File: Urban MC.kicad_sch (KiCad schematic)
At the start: 48 parts, among them J1 Conn_01x02, J2 Screw_Terminal_01x02, J3 Conn_01x02, J4 Conn_01x03, J5 Conn_01x02, J6 Screw_Terminal_01x03, SW1 SW_Push, U1 IRS2186, U1 MCP4725xxx-xCH, U2 IRS2186, U2 MCP2515-xSO, U3 IRS2186, U3 TJA1050, U4 IRF150P220XKMA1, U5 IRF150P220XKMA1, U6 IRF150P220XKMA1, U7 IRF150P220XKMA1, U8 IRF150P220XKMA1, U9 IRF150P220XKMA1

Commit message: added custom footprints
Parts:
- removed J6: Screw_Terminal_01x03, symbol Connector:Screw_Terminal_01x03
- added J10, J6, J7, J8, J9: Screw_Terminal_01x01, urban_mc_custom_footprints:WP-SHFU_7461100, symbol Connector:Screw_Terminal_01x01
- D1, D2: footprint (none) -> Diode_THT:D_DO-41_SOD81_P10.16mm_Horizontal
- HallConnectors1: renamed from J4; footprint (none) -> urban_mc_custom_footprints:CON_436500300_MOL
- HallPowerInput1: renamed from J5; footprint (none) -> urban_mc_custom_footprints:CON_436500200_MOL
- J1, J2, J3: footprint (none) -> urban_mc_custom_footprints:CON_436500200_MOL
- U10: footprint urban_mc_custom_footprints:CONV_LCW78_12-0.5 -> urban_mc_custom_footprints:CONV_LCW78_12-1.0
- U4, U5, U6, U7, U8, U9: footprint PG-TO247-3-901_INF -> urban_mc_custom_footprints:PG-TO247-3-901_INF
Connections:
- net +48V: now also J9.1 (Pin_1)
- net GND: now also J10.1 (Pin_1)
- net at R6.2, U6.3 (SOURCE), U7.2 (DRAIN): now also J7.1 (Pin_1)
- net at R7.2, U8.3 (SOURCE), U9.2 (DRAIN): now also J8.1 (Pin_1)
- net at R5.2, U4.3 (SOURCE), U5.2 (DRAIN): now also J6.1 (Pin_1)

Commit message: updated schematic
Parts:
- removed D2: D, Diode_THT:D_DO-41_SOD81_P10.16mm_Horizontal, symbol Device:D
- removed J7, J8: Screw_Terminal_01x01, urban_mc_custom_footprints:WP-SHFU_7461100, symbol Connector:Screw_Terminal_01x01
- removed U2: IRS2186, Package_SO:SOIC-8_3.9x4.9mm_P1.27mm, symbol Driver_FET:IRS2186
- added J4, J5: Screw_Terminal_01x01, urban_mc_custom_footprints:WP-SHFU_7461100, symbol Connector:Screw_Terminal_01x01
- added U14, U15, U16, U17, U18, U19, U2, U20, U21, U22, U24, U25, U26, U27, U28, U29, U30, U31: IQE022N06LM5CGSCATMA1, urban_mc_custom_footprints:IFX-PG-WHTFN-9-1-V, symbol IRF150P220:IRF150P220XKMA1
- added U23: IRS2186, Package_SO:SOIC-8_3.9x4.9mm_P1.27mm, symbol Driver_FET:IRS2186
- C11: value 1u -> 10u; footprint Capacitor_SMD:C_2220_5750Metric -> Capacitor_SMD:C_0805_2012Metric
- C8: value 10u -> 1u; footprint Capacitor_SMD:C_0805_2012Metric -> Capacitor_SMD:C_2220_5750Metric
- R3, R8: value 11Ω -> 2.4Ω; footprint Resistor_SMD:R_0402_1005Metric -> Resistor_SMD:R_0603_1608Metric
- R5, R6: value 2.4Ω -> 11Ω; footprint Resistor_SMD:R_0603_1608Metric -> Resistor_SMD:R_0402_1005Metric
- U1: value MCP4725xxx-xCH -> MCP4725
- U4, U5, U6, U7, U8, U9: value IRF150P220XKMA1 -> IQE022N06LM5CGSCATMA1; footprint urban_mc_custom_footprints:PG-TO247-3-901_INF -> urban_mc_custom_footprints:IFX-PG-WHTFN-9-1-V
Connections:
- net +12V: now also C1.2, U23.5 (VCC); no longer C8.2
- net +48V: now also U5.2 (DRAIN), U14.2 (DRAIN), U15.2 (DRAIN), U16.2 (DRAIN), U2.2 (DRAIN), U24.2 (DRAIN), U25.2 (DRAIN), U26.2 (DRAIN), U27.2 (DRAIN); no longer C11.1, C12.1, C13.1
- net GND: now also C1.1, C8.2, U17.3 (SOURCE), U18.3 (SOURCE), U19.3 (SOURCE), U20.3 (SOURCE), U21.3 (SOURCE), U22.3 (SOURCE), U23.3 (COM), U28.3 (SOURCE), U29.3 (SOURCE), U30.3 (SOURCE), U31.3 (SOURCE); no longer C11.2, C8.1, U5.3 (SOURCE)
- net at U1.8 (VB): now also C2.2; no longer C1.2
- net at R8.2: now also C12.1, J4.1 (Pin_1), U24.3 (SOURCE), U25.3 (SOURCE), U26.3 (SOURCE), U27.3 (SOURCE), U28.2 (DRAIN), U29.2 (DRAIN), U30.2 (DRAIN), U31.2 (DRAIN); no longer U6.1 (GATE)
- net at U6.3 (SOURCE), U7.2 (DRAIN): now also C8.1, R3.2, U4.3 (SOURCE), U5.3 (SOURCE), J5.1 (Pin_1), U2.3 (SOURCE), U20.2 (DRAIN), U21.2 (DRAIN), U22.2 (DRAIN); no longer R6.2
- net at A1.6 (D3): now also U1.1 (HIN)
- net at A1.8 (D5): now also U1.2 (LIN)
- net at R3.1: now also C2.1, U1.6 (VS)
- net at R6.1: now also U23.7 (HO); no longer C2.1
- net at R8.1: now also C11.1, U23.6 (VS)
- net at R4.2, U9.1 (GATE): now also U17.1 (GATE), U18.1 (GATE), U19.1 (GATE)
- net at R7.2, U8.3 (SOURCE), U9.2 (DRAIN): now also C13.1, J6.1 (Pin_1), U14.3 (SOURCE), U15.3 (SOURCE), U16.3 (SOURCE), U17.2 (DRAIN), U18.2 (DRAIN), U19.2 (DRAIN)
- net at R2.2, U5.1 (GATE): now also U4.1 (GATE), U6.1 (GATE), U2.1 (GATE)
- net at R9.1: now also U23.4 (LO); no longer U1.7 (HO)
- net at R9.2: now also U28.1 (GATE), U29.1 (GATE), U30.1 (GATE), U31.1 (GATE); no longer U4.1 (GATE)
- net at U7.1 (GATE): now also R5.2, U20.1 (GATE), U21.1 (GATE), U22.1 (GATE); no longer R3.2
- net at A1.12 (D9): now also U23.2 (LIN); no longer U1.2 (LIN)
- net at A1.9 (D6): now also U23.1 (HIN); no longer U1.1 (HIN)
- net at R10.2, U8.1 (GATE): now also U14.1 (GATE), U15.1 (GATE), U16.1 (GATE)
- net at U1.4 (LO): now also R5.1; no longer R2.1
- new net: R6.2, U24.1 (GATE), U25.1 (GATE), U26.1 (GATE), U27.1 (GATE)
- new net: C11.2, U23.8 (VB)
- new net: R2.1, U1.7 (HO)
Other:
- moved on the sheet: A1, C10, C13, C3, C4, C5, C6, C7, D1, HallConnectors1, HallPowerInput1, J1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

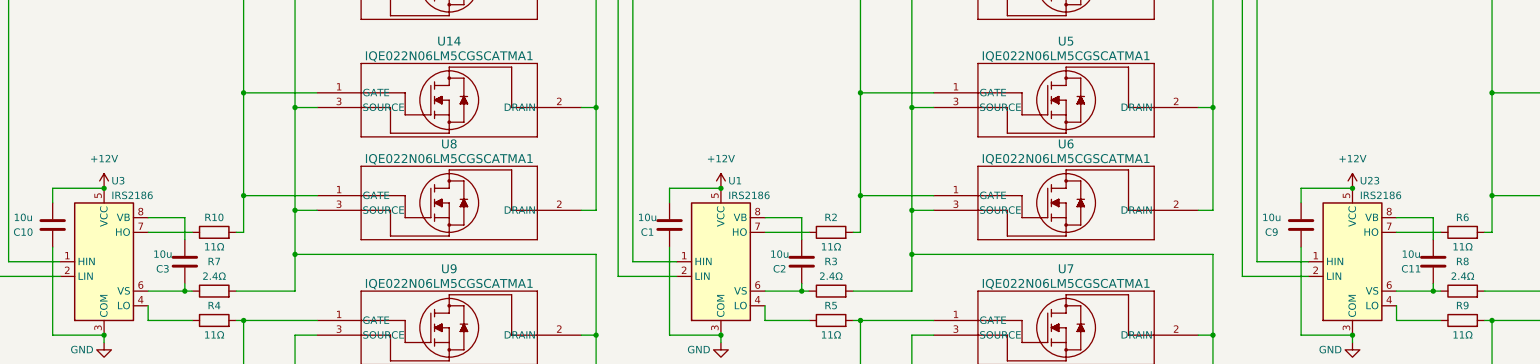
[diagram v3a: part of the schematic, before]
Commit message: Added diodes
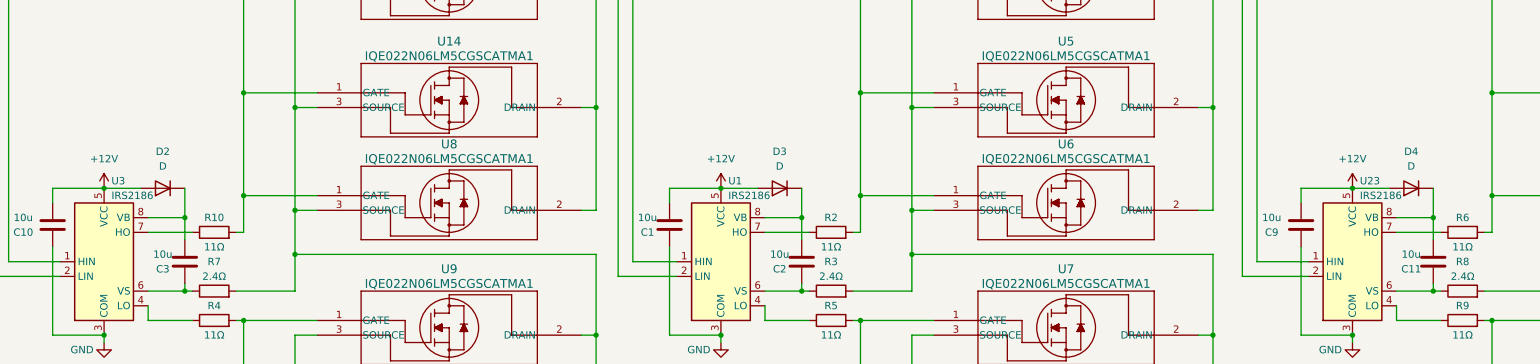
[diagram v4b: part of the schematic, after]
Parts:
- added D2, D3, D4: D, Diode_THT:D_DO-41_SOD81_P10.16mm_Horizontal, symbol Device:D
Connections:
- net +12V: now also D2.2 (A), D3.2 (A), D4.2 (A)
- net at C3.2, U3.8 (VB): now also D2.1 (K)
- net at C11.2, U23.8 (VB): now also D4.1 (K)
- net at C2.2, U1.8 (VB): now also D3.1 (K)

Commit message: Updated mosfet symbol
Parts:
- removed C1, C2: 10u, Capacitor_SMD:C_0805_2012Metric, symbol Device:C
- removed C13: 1u, Capacitor_SMD:C_2220_5750Metric, symbol Device:C
- removed R2: 11Ω, Resistor_SMD:R_0402_1005Metric, symbol Device:R
- removed R3: 2.4Ω, Resistor_SMD:R_0603_1608Metric, symbol Device:R
- removed U1, U23: IRS2186, Package_SO:SOIC-8_3.9x4.9mm_P1.27mm, symbol Driver_FET:IRS2186
- removed U14, U15, U17, U18, U19, U2, U20, U21, U22, U24, U25, U26, U27, U28, U29, U30, U31, U4, U5, U6, U7, U8, U9: IQE022N06LM5CGSCATMA1, urban_mc_custom_footprints:IFX-PG-WHTFN-9-1-V, symbol IRF150P220:IRF150P220XKMA1
- added C10, C7: 10u, Capacitor_SMD:C_0805_2012Metric, symbol Device:C
- added C6: 1u, Capacitor_SMD:C_2220_5750Metric, symbol Device:C
- added Q10, Q11, Q12, Q13, Q14, Q15, Q16, Q17, Q18, Q19, Q2, Q20, Q21, Q22, Q23, Q24, Q3, Q4, Q5, Q6, Q7, Q8, Q9: IQE022N06LM5CGSCATMA1, urban_mc_custom_footprints:IFX-PG-WHTFN-9-1-V, symbol Supermileage Symbols:root_0_IQE022N06LM5CGSC
- added R10, R7: 2.4Ω, Resistor_SMD:R_0603_1608Metric, symbol Device:R
- added U2, U3: IRS2186, Package_SO:SOIC-8_3.9x4.9mm_P1.27mm, symbol Driver_FET:IRS2186
- C8: value 1u -> 10u; footprint Capacitor_SMD:C_2220_5750Metric -> Capacitor_SMD:C_0805_2012Metric
- C9: value 10u -> 1u; footprint Capacitor_SMD:C_0805_2012Metric -> Capacitor_SMD:C_2220_5750Metric
- Q1: renamed from U16; symbol IRF150P220:IRF150P220XKMA1 -> Supermileage Symbols:root_0_IQE022N06LM5CGSC
- R8: value 2.4Ω -> 11Ω; footprint Resistor_SMD:R_0603_1608Metric -> Resistor_SMD:R_0402_1005Metric
- renumbered C4 to C1, C7 to C13, C5 to C2, C6 to C3, C10 to C4, C3 to C5, J9 to J4, J10 to J5, J4 to J6, J5 to J7, J6 to J8, R10 to R2, R7 to R3, U3 to U1
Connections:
- net +12V: now also C10.2, C7.2, U2.5 (VCC), U3.5 (VCC); no longer C9.2
- net +48V: now also Q1.5 (DRAIN1), Q1.6 (DRAIN2), Q1.7 (DRAIN3), Q1.8 (DRAIN4), Q11.5 (DRAIN1), Q11.6 (DRAIN2), Q11.7 (DRAIN3), Q11.8 (DRAIN4), Q13.5 (DRAIN1), Q13.6 (DRAIN2), Q13.7 (DRAIN3), Q13.8 (DRAIN4), Q15.5 (DRAIN1), Q15.6 (DRAIN2), Q15.7 (DRAIN3), Q15.8 (DRAIN4), Q17.5 (DRAIN1), Q17.6 (DRAIN2), Q17.7 (DRAIN3), Q17.8 (DRAIN4), Q19.5 (DRAIN1), Q19.6 (DRAIN2), Q19.7 (DRAIN3), Q19.8 (DRAIN4), Q2.5 (DRAIN1), Q2.6 (DRAIN2), Q2.7 (DRAIN3), Q2.8 (DRAIN4), Q21.5 (DRAIN1), Q21.6 (DRAIN2), Q21.7 (DRAIN3), Q21.8 (DRAIN4), Q23.5 (DRAIN1), Q23.6 (DRAIN2), Q23.7 (DRAIN3), Q23.8 (DRAIN4), Q3.5 (DRAIN1), Q3.6 (DRAIN2), Q3.7 (DRAIN3), Q3.8 (DRAIN4), Q4.5 (DRAIN1), Q4.6 (DRAIN2), Q4.7 (DRAIN3), Q4.8 (DRAIN4), Q9.5 (DRAIN1), Q9.6 (DRAIN2), Q9.7 (DRAIN3), Q9.8 (DRAIN4); no longer Q1.2 (DRAIN)
- net GND: now also C12.1, C10.1, C6.1, C7.1, Q10.1 (SOURCE1), Q10.2 (SOURCE2), Q10.3 (SOURCE3), Q10.4 (SOURCE4), Q12.1 (SOURCE1), Q12.2 (SOURCE2), Q12.3 (SOURCE3), Q12.4 (SOURCE4), Q14.1 (SOURCE1), Q14.2 (SOURCE2), Q14.3 (SOURCE3), Q14.4 (SOURCE4), Q16.1 (SOURCE1), Q16.2 (SOURCE2), Q16.3 (SOURCE3), Q16.4 (SOURCE4), Q18.1 (SOURCE1), Q18.2 (SOURCE2), Q18.3 (SOURCE3), Q18.4 (SOURCE4), Q20.1 (SOURCE1), Q20.2 (SOURCE2), Q20.3 (SOURCE3), Q20.4 (SOURCE4), Q22.1 (SOURCE1), Q22.2 (SOURCE2), Q22.3 (SOURCE3), Q22.4 (SOURCE4), Q24.1 (SOURCE1), Q24.2 (SOURCE2), Q24.3 (SOURCE3), Q24.4 (SOURCE4), Q5.1 (SOURCE1), Q5.2 (SOURCE2), Q5.3 (SOURCE3), Q5.4 (SOURCE4), Q6.1 (SOURCE1), Q6.2 (SOURCE2), Q6.3 (SOURCE3), Q6.4 (SOURCE4), Q7.1 (SOURCE1), Q7.2 (SOURCE2), Q7.3 (SOURCE3), Q7.4 (SOURCE4), Q8.1 (SOURCE1), Q8.2 (SOURCE2), Q8.3 (SOURCE3), Q8.4 (SOURCE4), U2.3 (COM), U3.3 (COM); no longer C12.2, C8.2
- net at R8.1: now also U3.4 (LO); no longer C11.1
- net at R6.2: now also Q11.9 (GATE), Q13.9 (GATE), Q15.9 (GATE), Q9.9 (GATE)
- net at R5.2: now also Q10.9 (GATE), Q12.9 (GATE), Q14.9 (GATE), Q16.9 (GATE)
- net at J7.1 (Pin_1): now also C9.2, Q10.5 (DRAIN1), Q10.6 (DRAIN2), Q10.7 (DRAIN3), Q10.8 (DRAIN4), Q11.1 (SOURCE1), Q11.2 (SOURCE2), Q11.3 (SOURCE3), Q11.4 (SOURCE4), Q12.5 (DRAIN1), Q12.6 (DRAIN2), Q12.7 (DRAIN3), Q12.8 (DRAIN4), Q13.1 (SOURCE1), Q13.2 (SOURCE2), Q13.3 (SOURCE3), Q13.4 (SOURCE4), Q14.5 (DRAIN1), Q14.6 (DRAIN2), Q14.7 (DRAIN3), Q14.8 (DRAIN4), Q15.1 (SOURCE1), Q15.2 (SOURCE2), Q15.3 (SOURCE3), Q15.4 (SOURCE4), Q16.5 (DRAIN1), Q16.6 (DRAIN2), Q16.7 (DRAIN3), Q16.8 (DRAIN4), Q9.1 (SOURCE1), Q9.2 (SOURCE2), Q9.3 (SOURCE3), Q9.4 (SOURCE4), R7.2; no longer C8.1
- net at R9.2: now also Q17.9 (GATE), Q19.9 (GATE), Q21.9 (GATE), Q23.9 (GATE)
- net at R5.1: now also U2.4 (LO)
- net at Q1.1 (SOURCE1): now also J8.1 (Pin_1), Q1.2 (SOURCE2), Q1.3 (SOURCE3), Q1.4 (SOURCE4), R3.2, C6.2, Q2.1 (SOURCE1), Q2.2 (SOURCE2), Q2.3 (SOURCE3), Q2.4 (SOURCE4), Q3.1 (SOURCE1), Q3.2 (SOURCE2), Q3.3 (SOURCE3), Q3.4 (SOURCE4), Q4.1 (SOURCE1), Q4.2 (SOURCE2), Q4.3 (SOURCE3), Q4.4 (SOURCE4), Q5.5 (DRAIN1), Q5.6 (DRAIN2), Q5.7 (DRAIN3), Q5.8 (DRAIN4), Q6.5 (DRAIN1), Q6.6 (DRAIN2), Q6.7 (DRAIN3), Q6.8 (DRAIN4), Q7.5 (DRAIN1), Q7.6 (DRAIN2), Q7.7 (DRAIN3), Q7.8 (DRAIN4), Q8.5 (DRAIN1), Q8.6 (DRAIN2), Q8.7 (DRAIN3), Q8.8 (DRAIN4); no longer R2.2
- net at A1.9 (D6): now also U3.1 (HIN)
- net at A1.12 (D9): now also U3.2 (LIN)
- net at R9.1: now also U3.7 (HO)
- net at R6.1: now also U2.7 (HO)
- net at C11.2, D4.1 (K): now also U3.8 (VB)
- net at R4.2: now also Q5.9 (GATE), Q6.9 (GATE), Q7.9 (GATE), Q8.9 (GATE)
- net at A1.6 (D3): now also U2.1 (HIN)
- net at A1.8 (D5): now also U2.2 (LIN)
- net at D3.1 (K): now also C8.2, U2.8 (VB)
- new net: C11.1, R10.1, U3.6 (VS)
- new net: Q1.9 (GATE), Q2.9 (GATE), Q3.9 (GATE), Q4.9 (GATE), R2.2
- new net: C12.2, J6.1 (Pin_1), Q17.1 (SOURCE1), Q17.2 (SOURCE2), Q17.3 (SOURCE3), Q17.4 (SOURCE4), Q18.5 (DRAIN1), Q18.6 (DRAIN2), Q18.7 (DRAIN3), Q18.8 (DRAIN4), Q19.1 (SOURCE1), Q19.2 (SOURCE2), Q19.3 (SOURCE3), Q19.4 (SOURCE4), Q20.5 (DRAIN1), Q20.6 (DRAIN2), Q20.7 (DRAIN3), Q20.8 (DRAIN4), Q21.1 (SOURCE1), Q21.2 (SOURCE2), Q21.3 (SOURCE3), Q21.4 (SOURCE4), Q22.5 (DRAIN1), Q22.6 (DRAIN2), Q22.7 (DRAIN3), Q22.8 (DRAIN4), Q23.1 (SOURCE1), Q23.2 (SOURCE2), Q23.3 (SOURCE3), Q23.4 (SOURCE4), Q24.5 (DRAIN1), Q24.6 (DRAIN2), Q24.7 (DRAIN3), Q24.8 (DRAIN4), R10.2
- new net: Q18.9 (GATE), Q20.9 (GATE), Q22.9 (GATE), Q24.9 (GATE), R8.2
- new net: C8.1, R7.1, U2.6 (VS)
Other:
- moved on the sheet: C4, C5, D2, J6, J7, J8, R2, R3, R4, U1

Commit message: mosfets
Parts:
- renumbered Q11 to Q10, Q13 to Q11, Q15 to Q12, Q10 to Q13, Q12 to Q14, Q14 to Q15, Q19 to Q18, Q21 to Q19, Q23 to Q20, Q18 to Q21, Q20 to Q22, Q22 to Q23
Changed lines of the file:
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@@
 		(on_board yes)
 		(dnp no)
-		(property "Reference" "Q10"
+		(property "Reference" "Q13"
 			(at 407.924 111.506 0)
 			(effects
@@
 			(project "Urban MC"
 				(path "/9c188f5e-4c43-43bc-b719-7c7a34d1ae77"
-					(reference "Q10")
+					(reference "Q13")
 					(unit 1)
 				)
@@
 		(on_board yes)
 		(dnp no)
-		(property "Reference" "Q11"
+		(property "Reference" "Q10"
 			(at 425.704 96.266 0)
 			(effects
@@
 			(project "Urban MC"
 				(path "/9c188f5e-4c43-43bc-b719-7c7a34d1ae77"
-					(reference "Q11")
+					(reference "Q10")
 					(unit 1)
 				)
@@
 		(on_board yes)
 		(dnp no)
-		(property "Reference" "Q15"
+		(property "Reference" "Q12"
 			(at 463.804 96.266 0)
 			(effects
@@
 			(project "Urban MC"
 				(path "/9c188f5e-4c43-43bc-b719-7c7a34d1ae77"
-					(reference "Q15")
+					(reference "Q12")
 					(unit 1)
 				)
@@
 		(on_board yes)
 		(dnp no)
-		(property "Reference" "Q23"
+		(property "Reference" "Q20"
 			(at 576.834 97.536 0)
 			(effects
@@
 			(project "Urban MC"
 				(path "/9c188f5e-4c43-43bc-b719-7c7a34d1ae77"
-					(reference "Q23")
+					(reference "Q20")
 					(unit 1)
 				)
@@
 		(on_board yes)
 		(dnp no)
-		(property "Reference" "Q19"
+		(property "Reference" "Q18"
 			(at 538.734 97.536 0)
 			(effects
@@
 			(project "Urban MC"
 				(path "/9c188f5e-4c43-43bc-b719-7c7a34d1ae77"
-					(reference "Q19")
+					(reference "Q18")
 					(unit 1)
 				)
@@
 		(on_board yes)
 		(dnp no)
-		(property "Reference" "Q12"
+		(property "Reference" "Q14"
 			(at 425.704 111.506 0)
 			(effects
@@
 			(project "Urban MC"
 				(path "/9c188f5e-4c43-43bc-b719-7c7a34d1ae77"
-					(reference "Q12")
+					(reference "Q14")
 					(unit 1)
 				)
@@
 		(on_board yes)
 		(dnp no)
-		(property "Reference" "Q18"
+		(property "Reference" "Q21"
 			(at 520.954 112.776 0)
 			(effects
@@
 			(project "Urban MC"
 				(path "/9c188f5e-4c43-43bc-b719-7c7a34d1ae77"
-					(reference "Q18")
+					(reference "Q21")
 					(unit 1)
 				)
@@
 		(on_board yes)
 		(dnp no)
-		(property "Reference" "Q13"
+		(property "Reference" "Q11"
 			(at 446.024 96.266 0)
 			(effects
@@
 			(project "Urban MC"
 				(path "/9c188f5e-4c43-43bc-b719-7c7a34d1ae77"
-					(reference "Q13")
+					(reference "Q11")
 					(unit 1)
 				)
@@
 		(on_board yes)
 		(dnp no)
-		(property "Reference" "Q22"
+		(property "Reference" "Q23"
 			(at 559.054 112.776 0)
 			(effects
@@
 			(project "Urban MC"
 				(path "/9c188f5e-4c43-43bc-b719-7c7a34d1ae77"
-					(reference "Q22")
+					(reference "Q23")
 					(unit 1)
 				)
@@
 		(on_board yes)
 		(dnp no)
-		(property "Reference" "Q14"
+		(property "Reference" "Q15"
 			(at 446.024 111.506 0)
 			(effects
@@
 			(project "Urban MC"
 				(path "/9c188f5e-4c43-43bc-b719-7c7a34d1ae77"
-					(reference "Q14")
+					(reference "Q15")
 					(unit 1)
 				)
@@
 		(on_board yes)
 		(dnp no)
-		(property "Reference" "Q21"
+		(property "Reference" "Q19"
 			(at 559.054 97.536 0)
 			(effects
@@
 			(project "Urban MC"
 				(path "/9c188f5e-4c43-43bc-b719-7c7a34d1ae77"
-					(reference "Q21")
+					(reference "Q19")
 					(unit 1)
 				)
@@
 		(on_board yes)
 		(dnp no)
-		(property "Reference" "Q20"
+		(property "Reference" "Q22"
 			(at 538.734 112.776 0)
 			(effects
@@
 			(project "Urban MC"
 				(path "/9c188f5e-4c43-43bc-b719-7c7a34d1ae77"
-					(reference "Q20")
+					(reference "Q22")
 					(unit 1)
 				)

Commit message: updated schematic and layout
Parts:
- removed C6, C9: 1u, Capacitor_SMD:C_2220_5750Metric, symbol Device:C
- removed C7, C8: 10u, Capacitor_SMD:C_0805_2012Metric, symbol Device:C
- removed D2, D3, D4: D, Diode_THT:D_DO-41_SOD81_P10.16mm_Horizontal, symbol Device:D
- removed J3: Conn_01x02, urban_mc_custom_footprints:CON_436500200_MOL, symbol Connector_Generic:Conn_01x02
- removed Q10, Q11, Q12, Q13, Q14, Q15, Q16, Q9: IQE022N06LM5CGSCATMA1, urban_mc_custom_footprints:IFX-PG-WHTFN-9-1-V, symbol Supermileage Symbols:root_0_IQE022N06LM5CGSC
- removed R1: 120, Resistor_SMD:R_0603_1608Metric, symbol Device:R
- removed R5, R6: 11Ω, Resistor_SMD:R_0402_1005Metric, symbol Device:R
- removed R7: 2.4Ω, Resistor_SMD:R_0603_1608Metric, symbol Device:R
- removed U2: IRS2186, Package_SO:SOIC-8_3.9x4.9mm_P1.27mm, symbol Driver_FET:IRS2186
- removed U3: TJA1050, Package_SO:SOIC-8_3.9x4.9mm_P1.27mm, symbol French Guy Projects:TJA1050
- added C1, C3, C4: 10u, Capacitor_SMD:C_0805_2012Metric, symbol Device:C
- added C2: 0.1uF, Capacitor_SMD:C_0805_2012Metric_Pad1.18x1.45mm_HandSolder, symbol Device:C_Small
- added C5: 1u, Capacitor_SMD:C_2220_5750Metric, symbol Device:C
- added C7, C9: 16pF, Capacitor_SMD:C_0805_2012Metric_Pad1.18x1.45mm_HandSolder, symbol Device:C_Small
- added D1, D2, D3: D, DIODE_DO214AA_MBRS_VIS, symbol Diode_Supermileage:SSB44-E3_52T
- added G1: IRS2186, Package_SO:SOIC-8_3.9x4.9mm_P1.27mm, symbol Driver_FET:IRS2186
- added Q1, Q2, Q3, Q4, Q5, Q6, Q7, Q8: IQE022N06LM5CGSCATMA1, urban_mc_custom_footprints:IFX-PG-WHTFN-9-1-V, symbol Supermileage Symbols:root_0_IQE022N06LM5CGSC
- added R1: 120, Resistor_SMD:R_0603_1608Metric, symbol Device:R_US
- added R2, R5: 11Ω, Resistor_SMD:R_0402_1005Metric, symbol Device:R_US
- added R3: 2.4Ω, Resistor_SMD:R_0603_1608Metric, symbol Device:R_US
- added R4: 10k, Resistor_SMD:R_0805_2012Metric_Pad1.20x1.40mm_HandSolder, symbol Device:R_US
- added SW1: CAN_TERM, Connector_PinHeader_2.54mm:PinHeader_1x02_P2.54mm_Horizontal, symbol Switch:SW_DIP_x01
- added U1: MCP2561/2, Package_SO:SOIC-8_3.9x4.9mm_P1.27mm, symbol Interface_CAN_LIN:MCP2551-I-SN
- added Y1: 8MHz, Crystal:Crystal_HC49-U_Vertical, symbol Device:Crystal
- C13: value 10u -> 1u; footprint Capacitor_SMD:C_0805_2012Metric -> Capacitor_SMD:C_2220_5750Metric
- D4: renamed from D1; footprint Diode_THT:D_DO-41_SOD81_P10.16mm_Horizontal -> urban_mc_custom_footprints:DO-201AD; symbol Device:D -> SR1204:SR1204; MANUFACTURER (none) -> Taiwan Semiconductor; MAXIMUM_PACKAGE_HEIGHT (none) -> 5.6 mm; PARTREV (none) -> K2105; STANDARD (none) -> IPC-7351B
- J2: value Screw_Terminal_01x02 -> Conn_01x02
- R10: renamed from R2; symbol Device:R -> Device:R_US
- R11: renamed from R3; symbol Device:R -> Device:R_US
- R12: renamed from R4; symbol Device:R -> Device:R_US
- R6: renamed from R1; symbol Device:R -> Device:R_US
- R7: renamed from R9; symbol Device:R -> Device:R_US
- R8: renamed from R10; symbol Device:R -> Device:R_US
- R9: renamed from R8; symbol Device:R -> Device:R_US
- renumbered C12 to C10, C4 to C11, C5 to C12, C1 to C14, C2 to C15, C3 to C16, C10 to C6, C11 to C8, U3 to G2, U1 to G3, J6 to J3, J7 to J4, J8 to J5, J4 to J6, J5 to J7, Q18 to Q10, Q19 to Q11, Q20 to Q12, Q21 to Q13, Q22 to Q14, Q23 to Q15, Q24 to Q16, Q1 to Q17, Q2 to Q18, Q3 to Q19, Q4 to Q20, Q5 to Q21, Q6 to Q22, Q7 to Q23, Q8 to Q24, Q17 to Q9, SW1 to SW2, U10 to U4
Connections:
- net +12V: now also C1.1, C3.2, D1.2, D2.2, D3.2, G1.5 (VCC)
- net +48V: now also D4.A, Q1.5 (DRAIN1), Q1.6 (DRAIN2), Q1.7 (DRAIN3), Q1.8 (DRAIN4), Q2.5 (DRAIN1), Q2.6 (DRAIN2), Q2.7 (DRAIN3), Q2.8 (DRAIN4), Q3.5 (DRAIN1), Q3.6 (DRAIN2), Q3.7 (DRAIN3), Q3.8 (DRAIN4), Q4.5 (DRAIN1), Q4.6 (DRAIN2), Q4.7 (DRAIN3), Q4.8 (DRAIN4); no longer D4.2 (A)
- net +5V: now also A1.27 (+5V), C2.2, U1.3 (VDD); no longer C13.1
- net CAN HIGH: now also U1.7 (CANH); no longer J1.2 (Pin_2)
- net CAN LOW: now also J1.2 (Pin_2), R1.1, U1.6 (CANL)
- net GND: now also C13.1, C1.2, C2.1, C3.1, C5.1, C7.1, C9.1, G1.3 (COM), Q5.1 (SOURCE1), Q5.2 (SOURCE2), Q5.3 (SOURCE3), Q5.4 (SOURCE4), Q6.1 (SOURCE1), Q6.2 (SOURCE2), Q6.3 (SOURCE3), Q6.4 (SOURCE4), Q7.1 (SOURCE1), Q7.2 (SOURCE2), Q7.3 (SOURCE3), Q7.4 (SOURCE4), Q8.1 (SOURCE1), Q8.2 (SOURCE2), Q8.3 (SOURCE3), Q8.4 (SOURCE4), R4.2, U1.2 (VSS); no longer C13.2
- net at C8.2, G2.8 (VB): now also D2.1
- net at J5.1 (Pin_1), Q17.1 (SOURCE1), Q17.2 (SOURCE2)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: now also C13.2
- net at J4.1 (Pin_1): now also C10.2, Q10.1 (SOURCE1), Q10.2 (SOURCE2), Q10.3 (SOURCE3), Q10.4 (SOURCE4), Q11.1 (SOURCE1), Q11.2 (SOURCE2), Q11.3 (SOURCE3), Q11.4 (SOURCE4), Q12.1 (SOURCE1), Q12.2 (SOURCE2), Q12.3 (SOURCE3), Q12.4 (SOURCE4), Q13.5 (DRAIN1), Q13.6 (DRAIN2), Q13.7 (DRAIN3), Q13.8 (DRAIN4), Q14.5 (DRAIN1), Q14.6 (DRAIN2), Q14.7 (DRAIN3), Q14.8 (DRAIN4), Q15.5 (DRAIN1), Q15.6 (DRAIN2), Q15.7 (DRAIN3), Q15.8 (DRAIN4), Q16.5 (DRAIN1), Q16.6 (DRAIN2), Q16.7 (DRAIN3), Q16.8 (DRAIN4), Q9.1 (SOURCE1), Q9.2 (SOURCE2), Q9.3 (SOURCE3), Q9.4 (SOURCE4), R8.2
- net at J1.1 (Pin_1): now also SW1.2
- net at C12.2, G3.8 (VB): now also D3.1
- net at U2.1 (TXCAN): now also U1.1 (TXD)
- net at U2.2 (RXCAN): now also U1.4 (RXD)
- net at A1.6 (D3): now also G1.1 (HIN)
- net at A1.8 (D5): now also G1.2 (LIN)
- net at U4.1 (VIN): now also D4.C; no longer D4.1 (K)
- net C+: now reaches U2.7 (OSC2)
- net C+: now also C7.2, Y1.1
- net C-: now reaches U2.8 (OSC1)
- net C-: now also C9.2, Y1.2
- new net: C5.2, J3.1 (Pin_1), Q1.1 (SOURCE1), Q1.2 (SOURCE2), Q1.3 (SOURCE3), Q1.4 (SOURCE4), Q2.1 (SOURCE1), Q2.2 (SOURCE2), Q2.3 (SOURCE3), Q2.4 (SOURCE4), Q3.1 (SOURCE1), Q3.2 (SOURCE2), Q3.3 (SOURCE3), Q3.4 (SOURCE4), Q4.1 (SOURCE1), Q4.2 (SOURCE2), Q4.3 (SOURCE3), Q4.4 (SOURCE4), Q5.5 (DRAIN1), Q5.6 (DRAIN2), Q5.7 (DRAIN3), Q5.8 (DRAIN4), Q6.5 (DRAIN1), Q6.6 (DRAIN2), Q6.7 (DRAIN3), Q6.8 (DRAIN4), Q7.5 (DRAIN1), Q7.6 (DRAIN2), Q7.7 (DRAIN3), Q7.8 (DRAIN4), Q8.5 (DRAIN1), Q8.6 (DRAIN2), Q8.7 (DRAIN3), Q8.8 (DRAIN4), R3.2
- new net: Q5.9 (GATE), Q6.9 (GATE), Q7.9 (GATE), Q8.9 (GATE), R5.2
- new net: C4.2, D1.1, G1.8 (VB)
- new net: C4.1, G1.6 (VS), R3.1
- new net: R1.2, SW1.1
- new net: R4.1, U1.8 (Rs)
- new net: G1.7 (HO), R2.1
- new net: Q1.9 (GATE), Q3.9 (GATE), Q4.9 (GATE), R2.2
- new net: G1.4 (LO), R5.1
- no-connect marks 47 -> 45
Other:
- moved on the sheet: A1, C10, C11, C12, C14, C15, C16, C6, C8, G2, G3, HallConnectors1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

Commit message: Updated Connectors from Metal Screw to Screw Terminal
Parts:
- removed J3, J4, J5, J6, J7: Screw_Terminal_01x01, urban_mc_custom_footprints:WP-SHFU_7461100, symbol Connector:Screw_Terminal_01x01
- added J3: Conn_01x03, urban_mc_custom_footprints:TE_1986660-3, symbol Connector_Generic:Conn_01x03
- added J4: Conn_01x02, urban_mc_custom_footprints:TE_1-1986660-2, symbol Connector_Generic:Conn_01x02
- J2: symbol Connector:Screw_Terminal_01x02 -> Connector_Generic:Conn_01x02
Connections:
- net +48V: now also J4.1 (Pin_1)
- net GND: now also J4.2 (Pin_2)
- net at C5.2, Q1.1 (SOURCE1), Q1.2 (SOURCE2)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: now also J3.1 (Pin_1)
- net at C13.2, Q17.1 (SOURCE1), Q17.2 (SOURCE2)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: now also J3.3 (Pin_3)
- net at C10.2, Q10.1 (SOURCE1), Q10.2 (SOURCE2)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: now also J3.2 (Pin_2)
